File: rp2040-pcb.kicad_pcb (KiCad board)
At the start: 2 copper layers, 43 parts, among them J1 Conn_01x20_Male, J2 Conn_01x20_Male, J3 USB_C_Receptacle, SW1 SW_Push, SW2 SW_Push, U1 TPS54202DDC, U2 W25Q128JVSIQ, U3 RP2040, Y1 12 MHz

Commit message: Moved components roughly in place.
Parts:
- moved R9 387.8 mm to (68.6, 152.4)
- moved R10 361.2 mm to (106.7, 154.9)
- moved R11 359.6 mm to (111.8, 154.9)
- moved R6 359.1 mm to (109.7, 149.9)
- moved SW1 351.3 mm to (81.3, 142.2)
- moved R5 347.0 mm to (106.7, 149.9)
- moved C1 339.2 mm to (70.8, 43.2)
- moved J3 332.1 mm to (96.5, 152.4)
- moved SW2 329.7 mm to (81.1, 152.4)
- moved C13 327.5 mm to (87.8, 73.7)
- moved C4 325.4 mm to (74.6, 34.8)
- moved R1 322.6 mm to (73.7, 30.5)
- moved R3 322.4 mm to (81.7, 30.5)
- moved PWR_LED1 322.3 mm to (83.6, 37.7)
- moved R2 322.0 mm to (77.1, 30.5)
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
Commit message: Updated numbering. Updated USB footpring on PCB.
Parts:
- J3: value USB_C_Receptacle -> 105450-0101; footprint Connector_USB:USB_C_Receptacle_Palconn_UTC16-G -> Filips_Footprints:MOLEX_105450-0101
- moved C8 34.5 mm to (100.5, 99.3), turned to 90 degrees
- moved C9 33.3 mm to (102.8, 98.5), turned to 90 degrees
- moved C7 29.0 mm to (96.1, 94.0)
- moved J3 1.73 mm to (98.2, 152.5)
- moved U1 1.73 mm to (100.8, 105.3), turned to 0 degrees
- renumbered U3 to U1, U1 to U2, U2 to U3
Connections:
- R10 pad 1: Net-(J3-PadB5) -> GND
- R10 pad 2: GND -> Net-(J3-PadA5)
- R11 pad 1: Net-(J3-PadA5) -> GND
- R11 pad 2: GND -> Net-(J3-PadB5)

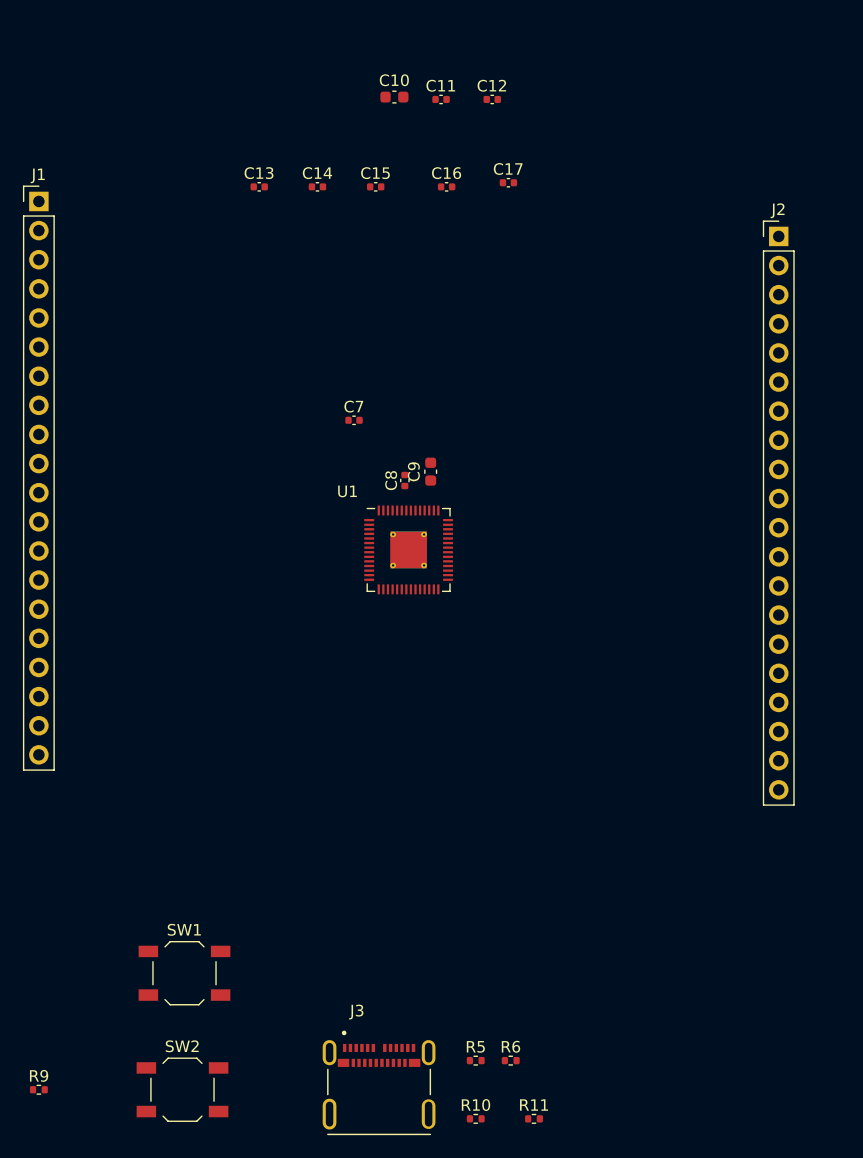
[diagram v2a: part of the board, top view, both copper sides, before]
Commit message: Aligned RP and headers.
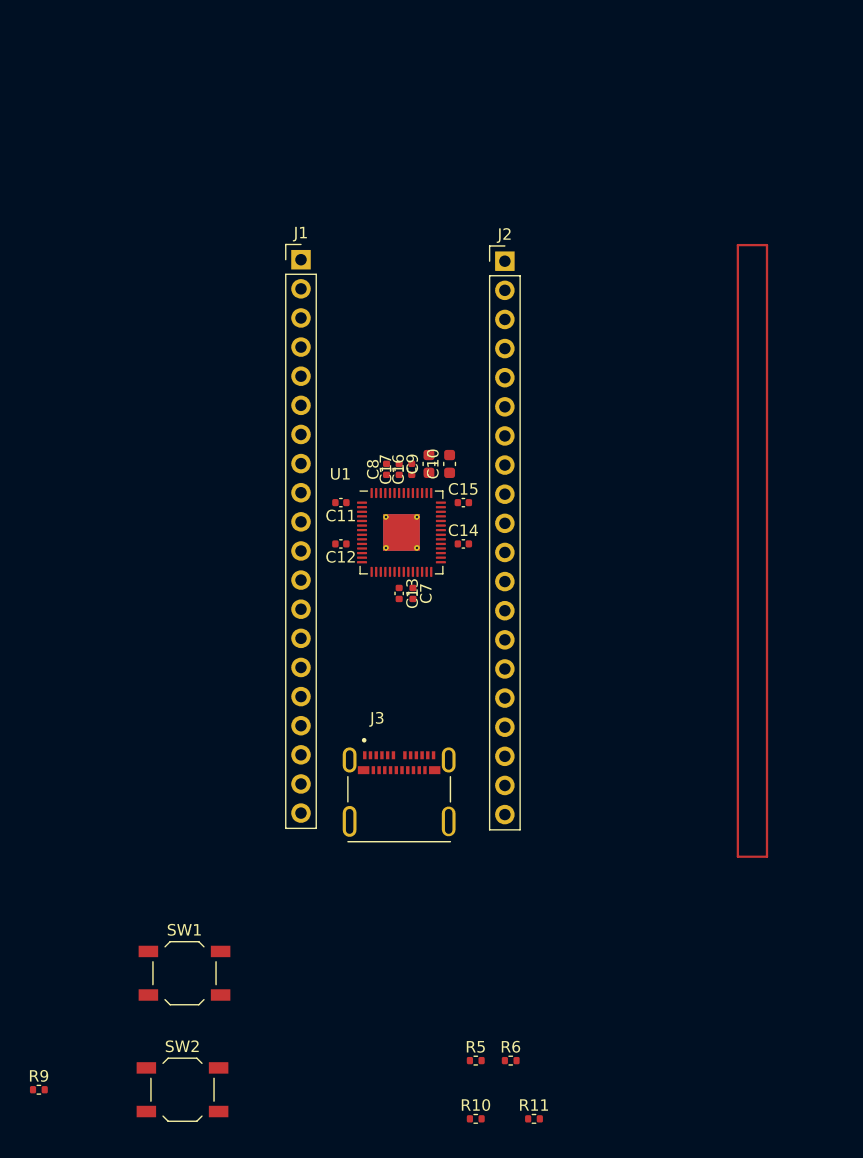
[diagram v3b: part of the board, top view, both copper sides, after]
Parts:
- moved C12 40.9 mm to (94.9, 104.8), turned to 180 degrees
- moved C13 37.5 mm to (100.0, 109.1), turned to -90 degrees
- moved C11 36.2 mm to (94.9, 101.2), turned to 180 degrees
- moved C14 33.6 mm to (105.6, 104.8)
- moved C10 32.4 mm to (104.4, 97.8), turned to 90 degrees
- moved C15 28.6 mm to (105.6, 101.2)
- moved C17 26.8 mm to (100.0, 98.3), turned to 90 degrees
- moved J3 25.6 mm to (100.0, 127.0)
- moved C16 24.8 mm to (101.1, 98.3), turned to 90 degrees
- moved J2 24.0 mm to (109.2, 80.1)
- moved J1 23.4 mm to (91.4, 80.0)
- moved C7 15.9 mm to (101.2, 109.1), turned to -90 degrees
- moved C8 1.87 mm to (98.9, 98.3)
- moved U1 1.65 mm to (100.2, 103.8)
- moved C9 0.69 mm to (102.6, 97.8)

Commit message: Board outline
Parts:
- moved J3 45.8 mm to (100.3, 81.2), turned to 180 degrees
- moved J2 1.40 mm to (109.2, 78.7)
- moved C13 1.27 mm to (100.0, 107.8)
- moved C7 1.27 mm to (101.2, 107.8)
- moved C10 1.27 mm to (104.4, 96.6)
- moved C11 1.27 mm to (94.9, 99.9)
- moved C12 1.27 mm to (94.9, 103.5)
- moved C14 1.27 mm to (105.6, 103.5)
- moved C15 1.27 mm to (105.6, 99.9)
- moved C16 1.27 mm to (101.1, 97.0)
- moved C17 1.27 mm to (100.0, 97.0)
- moved C8 1.27 mm to (98.9, 97.0)
- moved C9 1.27 mm to (102.6, 96.6)
- moved J1 1.27 mm to (91.4, 78.7)
- moved U1 1.27 mm to (100.2, 102.5)
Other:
- board outline added: 20.7 x 51.2 mm

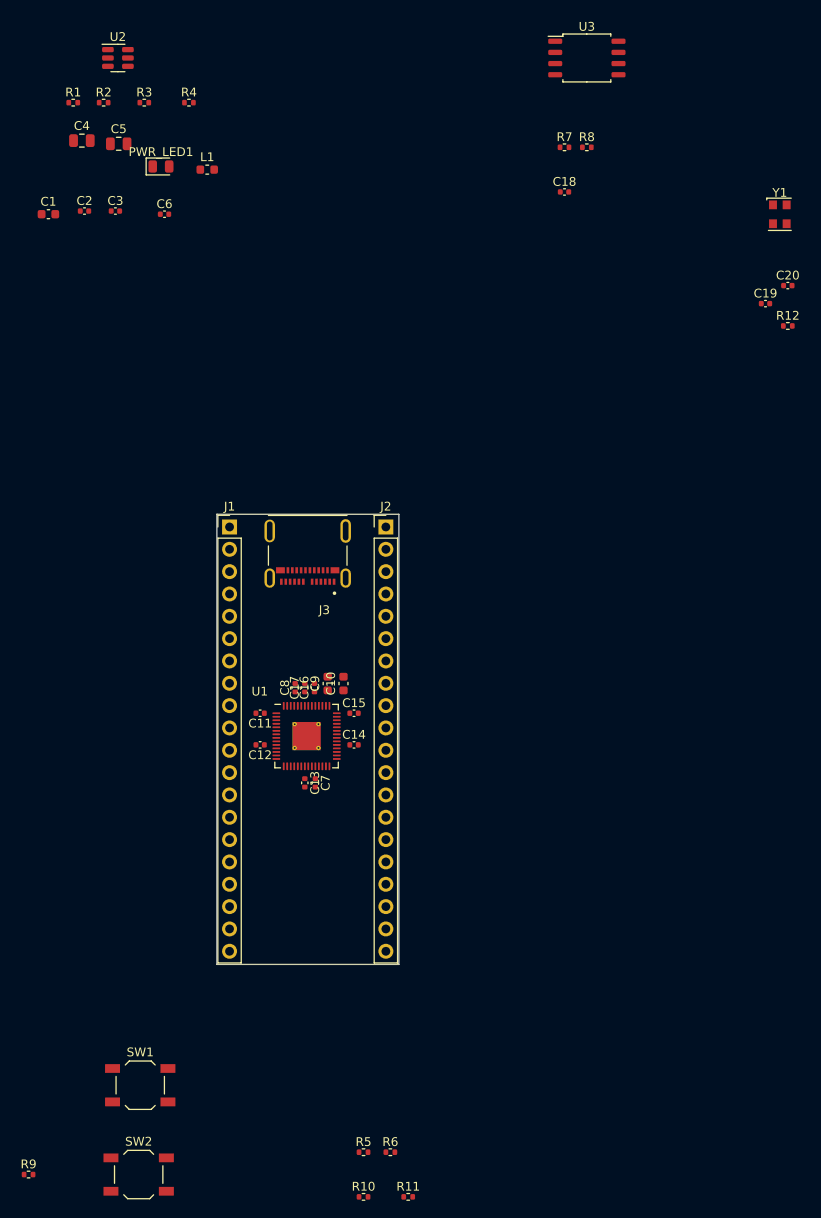
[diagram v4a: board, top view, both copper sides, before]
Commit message: more components placed
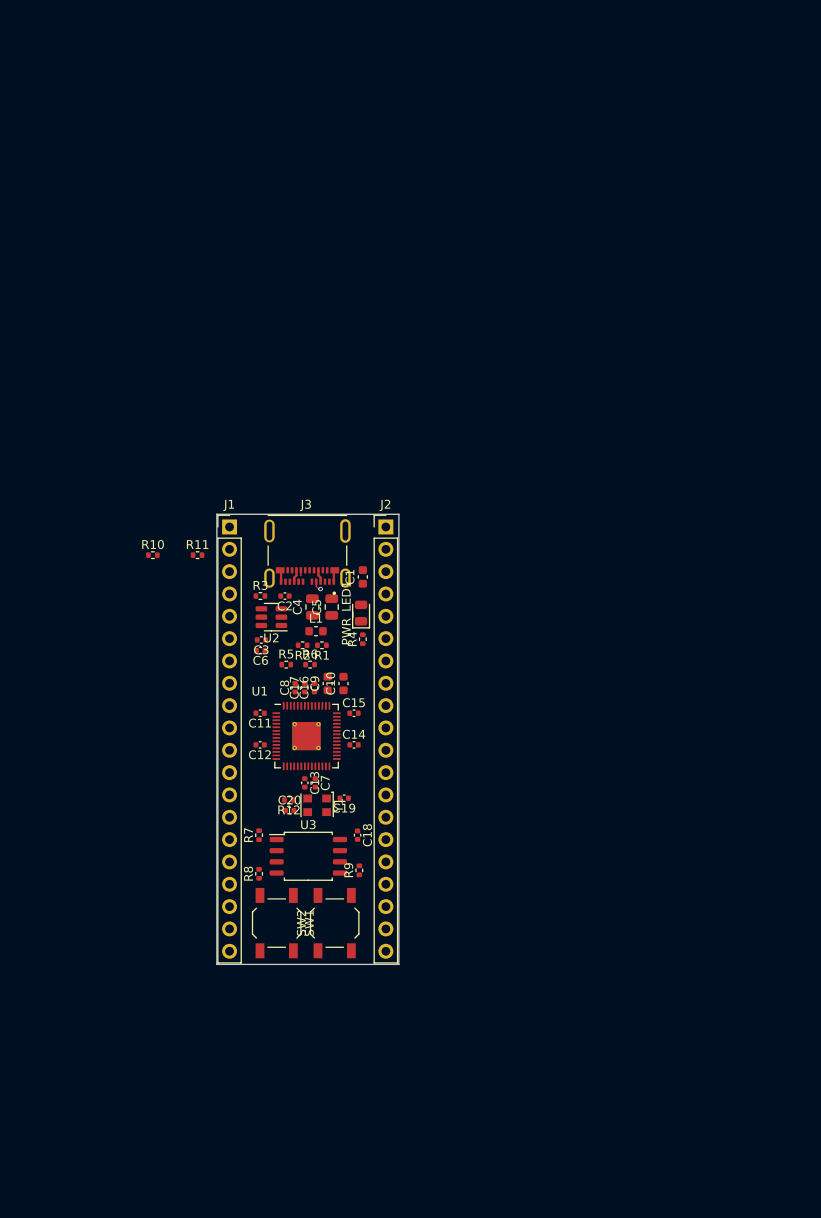
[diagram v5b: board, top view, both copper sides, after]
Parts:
- moved U3 96.2 mm to (100.4, 116.2)
- moved R8 90.7 mm to (94.8, 118.2), turned to 90 degrees
- moved R7 85.6 mm to (94.8, 113.8), turned to 90 degrees
- moved Y1 85.4 mm to (101.4, 110.4), turned to -90 degrees
- moved C20 82.3 mm to (98.3, 111.0)
- moved R12 78.3 mm to (98.2, 109.8), turned to 180 degrees
- moved C18 76.9 mm to (106.0, 113.8), turned to -90 degrees
- moved R10 76.8 mm to (82.7, 82.0)
- moved R11 76.8 mm to (87.8, 82.0)
- moved C19 73.9 mm to (104.5, 109.6), turned to 180 degrees
- moved R1 67.9 mm to (102.0, 92.2), turned to 180 degrees
- moved U2 66.0 mm to (96.2, 89.0), turned to 180 degrees
- moved R2 65.7 mm to (99.8, 92.2), turned to 180 degrees
- moved R4 64.2 mm to (106.6, 91.5), turned to 90 degrees
- moved C4 59.2 mm to (100.9, 87.8), turned to 90 degrees
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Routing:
- net VCC: track 0.00 -> 2.81 mm
- net GND: track 0.00 -> 2.68 mm
- net Net-(J3-PadA5): track 0.00 -> 1.17 mm, vias 0 -> 1
- net Net-(J3-PadB5): track 0.00 -> 0.65 mm

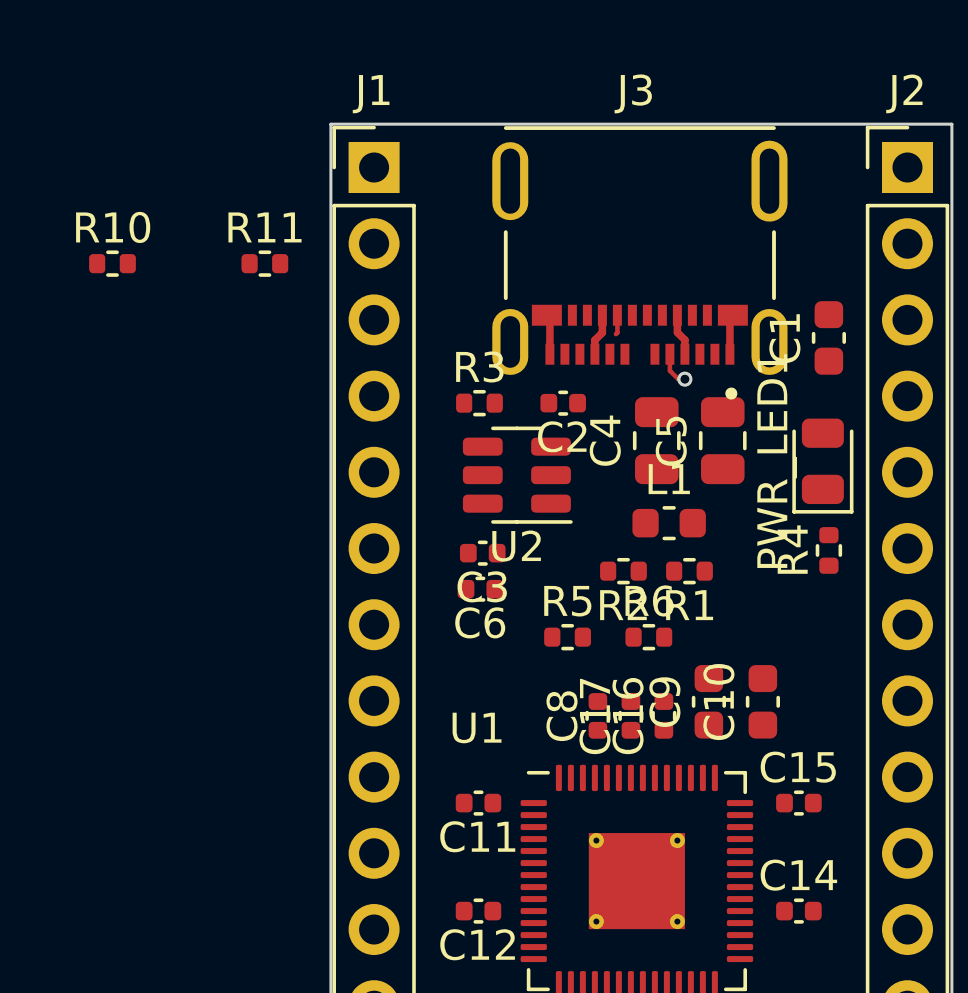
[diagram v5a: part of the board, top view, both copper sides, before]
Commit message: Routed USB.
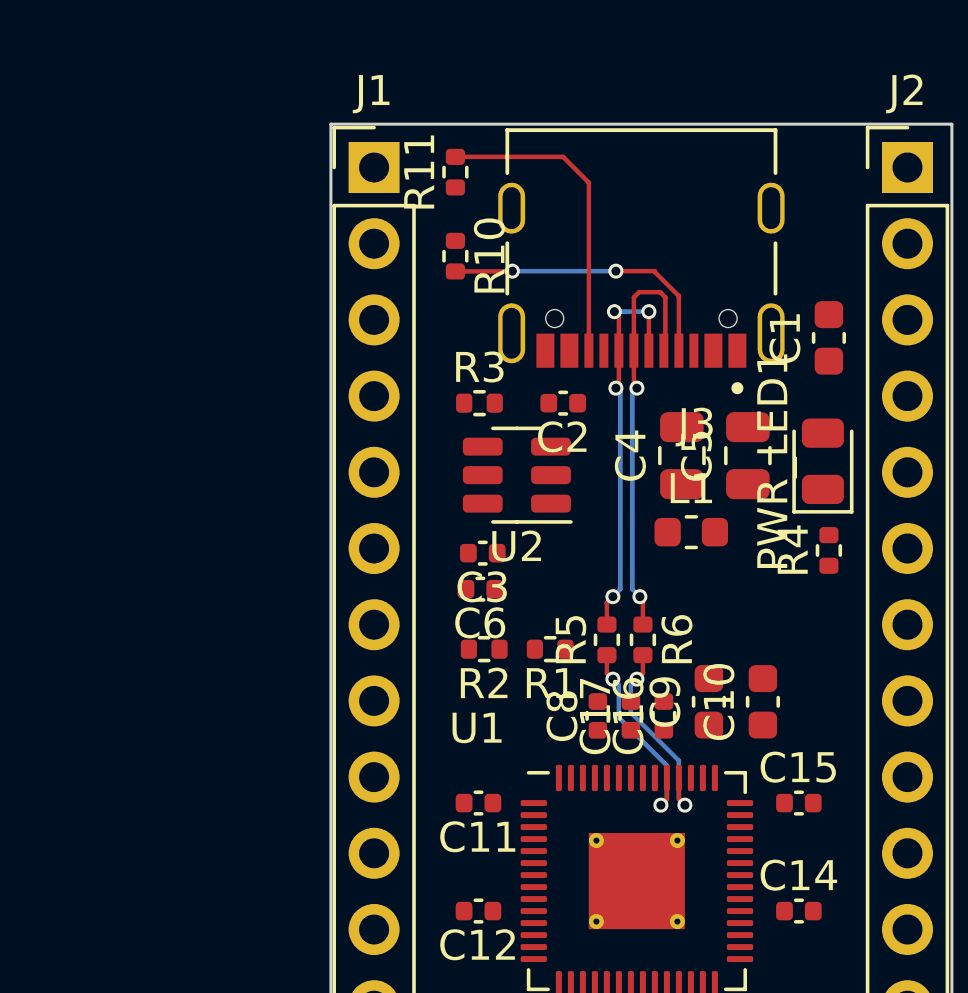
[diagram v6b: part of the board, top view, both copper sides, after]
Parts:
- J3: value 105450-0101 -> TYPE-C-31-M-12; footprint Filips_Footprints:MOLEX_105450-0101 -> TYPE-C-31-M-12:HRO_TYPE-C-31-M-12
- moved R10 11.4 mm to (94.2, 81.7), turned to -90 degrees
- moved R11 7.04 mm to (94.2, 78.9), turned to 90 degrees
- moved R1 5.32 mm to (97.3, 94.8)
- moved R2 5.32 mm to (95.1, 94.8)
- moved R5 1.31 mm to (99.2, 94.5), turned to 90 degrees
- moved J3 1.10 mm to (100.3, 80.1)
- moved C4 0.98 mm to (101.7, 88.3)
- moved C5 0.98 mm to (103.9, 88.3)
- moved L1 0.80 mm to (102.0, 90.9)
- moved R6 0.22 mm to (100.4, 94.5), turned to -90 degrees
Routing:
- net USB D-: track 0.00 -> 14.1 mm, vias 0 -> 2
- net USB D+: track 0.00 -> 13.2 mm, vias 0 -> 4
- net Net-(R11-Pad2): track 0.65 -> 10.4 mm
- net Net-(R10-Pad2): track 1.17 -> 9.65 mm, vias 1 -> 2
- net /N_USB_D-: track 0.00 -> 6.87 mm, vias 0 -> 2
- net /N_USB_D+: track 0.00 -> 6.87 mm, vias 0 -> 2
- net VCC: track 2.81 -> 0.00 mm
- net GND: track 2.68 -> 0.00 mm

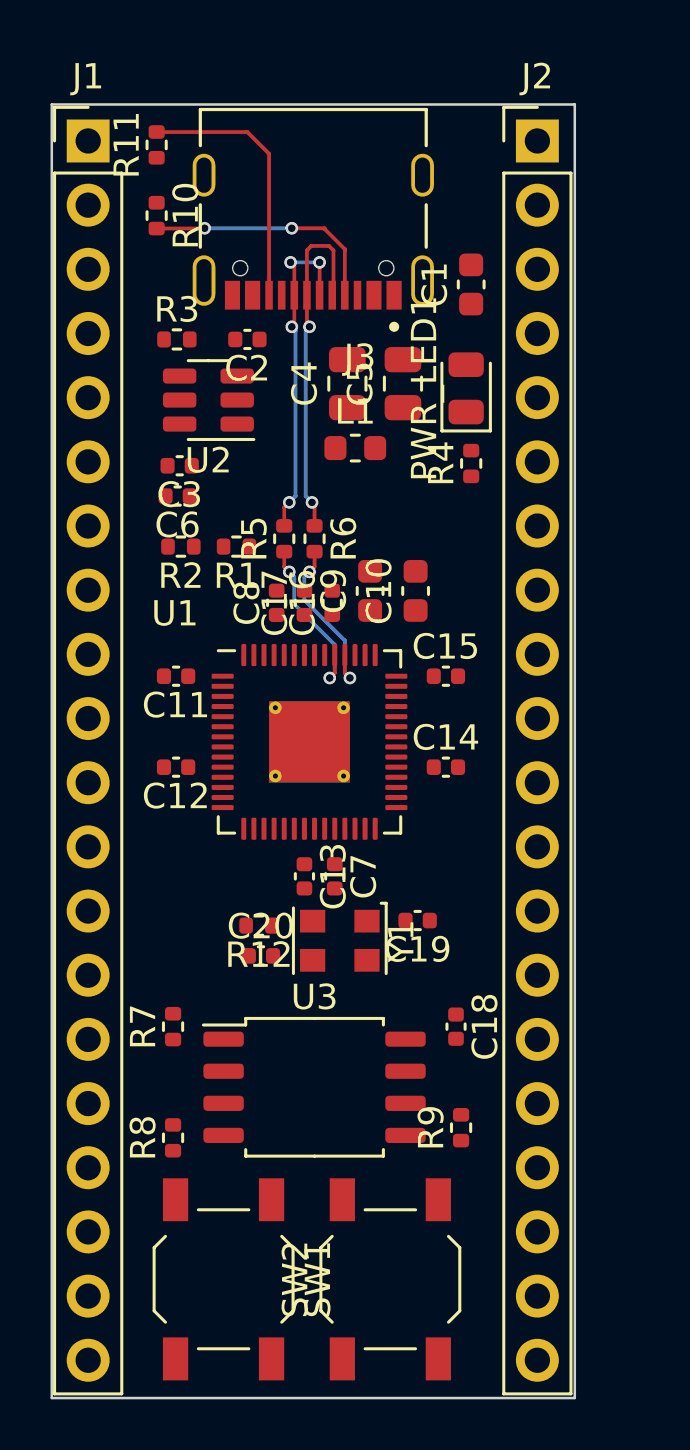
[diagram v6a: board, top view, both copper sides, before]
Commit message: Made board a bit bigger.
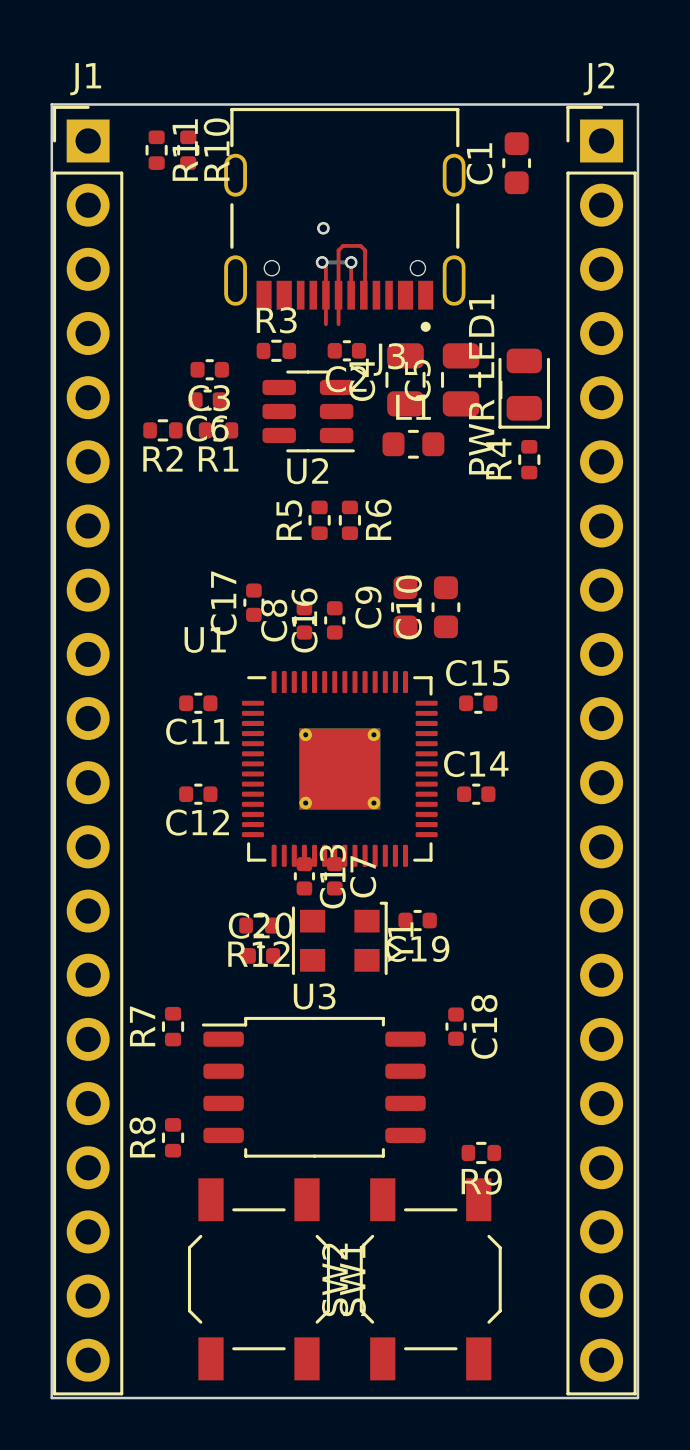
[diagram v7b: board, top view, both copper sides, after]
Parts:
- moved C1 5.13 mm to (108.4, 79.6)
- moved R1 4.65 mm to (96.6, 90.2)
- moved R2 4.65 mm to (94.4, 90.2)
- moved C3 3.98 mm to (96.2, 87.8)
- moved C6 3.98 mm to (96.2, 89.0)
- moved C2 3.96 mm to (101.7, 87.0)
- moved R3 3.96 mm to (98.9, 87.0)
- moved U2 3.96 mm to (100.1, 89.5)
- moved R10 2.88 mm to (95.4, 79.1)
- moved J2 2.54 mm to (111.8, 78.7)
- moved R4 2.30 mm to (108.9, 91.4)
- moved L1 2.30 mm to (104.3, 90.8)
- moved C4 2.30 mm to (104.0, 88.2)
- moved C5 2.30 mm to (106.2, 88.2)
- moved PWR_LED1 2.30 mm to (108.7, 88.4)
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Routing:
- net Net-(R11-Pad2): track 10.4 -> 0.00 mm
- net Net-(R10-Pad2): track 9.65 -> 0.00 mm, vias 2 -> 1
- net USB D+: track 13.2 -> 4.96 mm, vias 4 -> 2
- net USB D-: track 14.1 -> 5.92 mm, vias 2 -> 0
- net /N_USB_D-: track 6.87 -> 0.00 mm, vias 2 -> 0
- net /N_USB_D+: track 6.87 -> 0.00 mm, vias 2 -> 0
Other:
- board size 20.7 x 51.2 mm -> 23.2 x 51.2 mm
